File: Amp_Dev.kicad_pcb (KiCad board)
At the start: 2 copper layers, 100 x 100 mm, 508 parts, among them J1 SMA, J10 SMA, J11 CONN_01X02, J12 TEST_1P, J13 SMA, J14 CONN_01X02, J16 TEST_1P, J17 TEST_1P, J18 TEST_1P, J2 SMA, J20 SMA, J21 SMA, J22 SMA, J3 TEST_1P, J4 TEST_1P, J5 CONN_01X03, J6 TEST_1P, J7 CONN_01X03, J8 TEST_1P, J9 TEST_1P, Q1 DMN2075U, U1 MML09211H, U2 RF6886, U3 LMV358, U4 SN74LVC1G17, U5 TLV702, U6 LTC2644, U7 RT9183

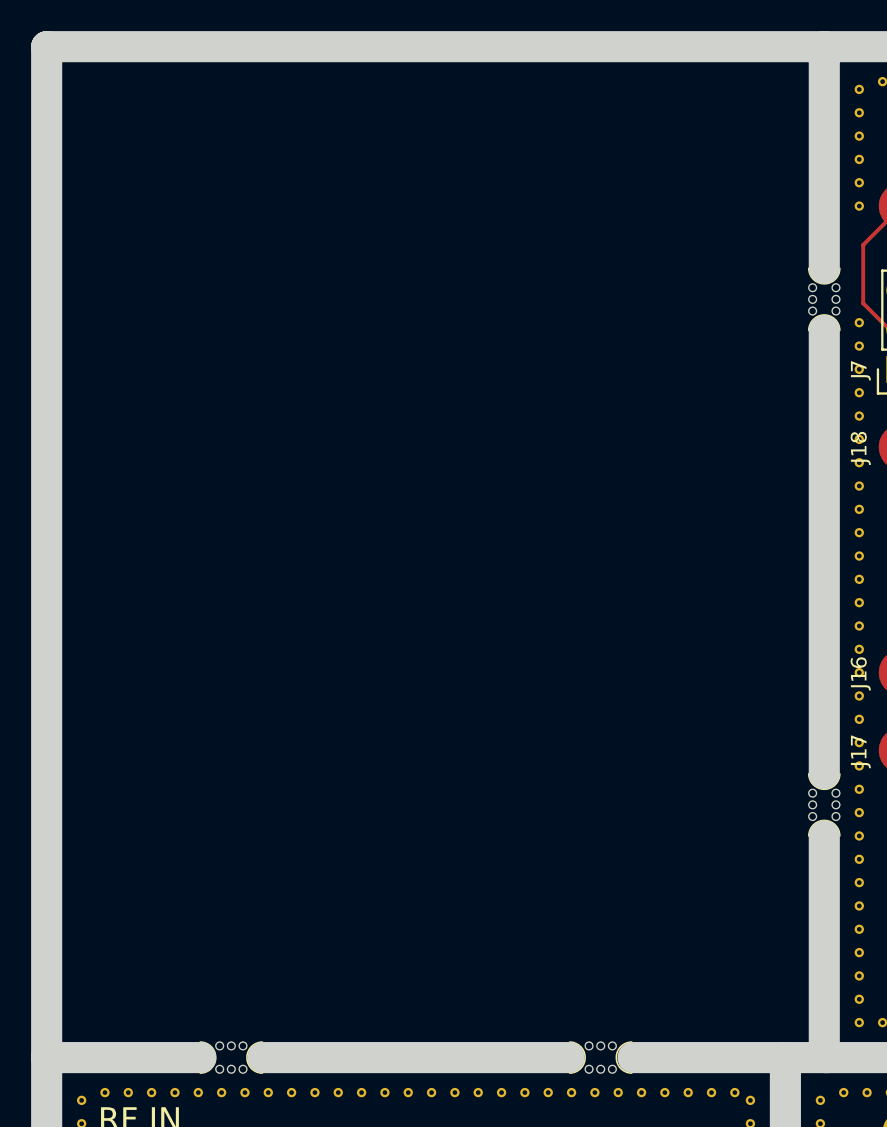
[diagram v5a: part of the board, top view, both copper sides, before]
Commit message: Added silkscreen and another PA board
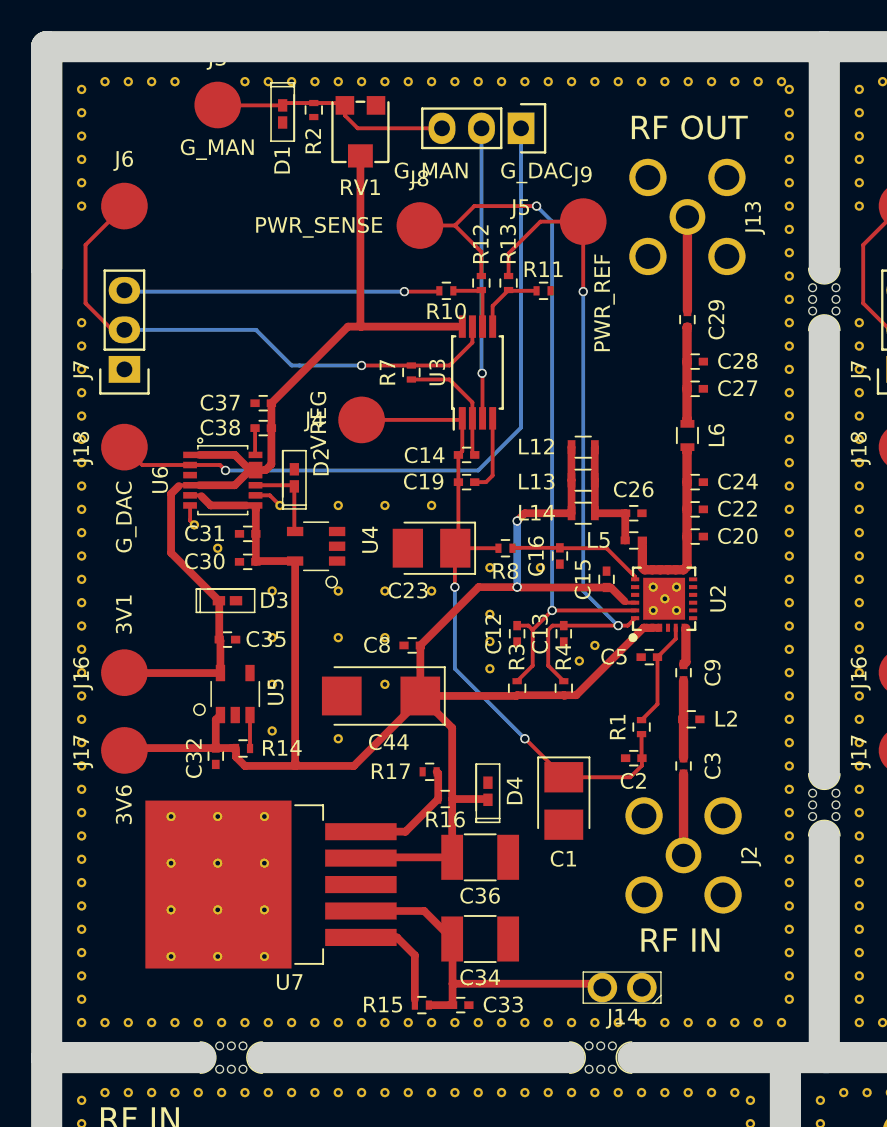
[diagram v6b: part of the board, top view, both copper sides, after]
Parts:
- added C1: 10uF, SFUSat:CP_Tantalum_Case-B_EIA-1411-21_Reflow, F.Cu at (133.2, 98.5)
- added C12: 1uF, SFUSat:C_0402, F.Cu at (130.2, 87.8)
- added C13: 1uF, SFUSat:C_0402, F.Cu at (133.2, 87.8)
- added C14: 0.1uF, SFUSat:C_0402, F.Cu at (127.0, 76.2)
- added C15: 1uF, SFUSat:C_0402, F.Cu at (136.0, 84.2)
- added C16: 2.2uF, SFUSat:C_0402, F.Cu at (133.0, 82.8)
- added C19: 1uF, SFUSat:C_0402, F.Cu at (127.0, 78.0)
- added C2: 1uF, SFUSat:C_0402, F.Cu at (137.8, 95.8)
- added C20: DNP, SFUSat:C_0402, F.Cu at (141.7, 81.5)
- added C22: 10pF, SFUSat:C_0402, F.Cu at (141.7, 79.8)
- added C23: 10uF, SFUSat:CP_Tantalum_Case-B_EIA-1411-21_Reflow, F.Cu at (124.8, 82.2)
- added C24: 27pF, SFUSat:C_0402, F.Cu at (141.7, 78.0)
- added C26: 2.2uF, SFUSat:C_0402, F.Cu at (137.8, 80.0)
- added C27: 10pF, SFUSat:C_0402, F.Cu at (141.7, 72.0)
- added C28: 1.2pF, SFUSat:C_0402, F.Cu at (141.7, 70.2)
- added C29: 100pF, SFUSat:C_0402, F.Cu at (141.2, 67.5)
- added C3: 100pF, SFUSat:C_0402, F.Cu at (140.9, 96.2)
- added C30: 0.1uF, SFUSat:C_0402, F.Cu at (112.9, 83.1)
- added C31: 0.1uF, SFUSat:C_0402, F.Cu at (112.9, 81.3)
- added C32: 1uF, SFUSat:C_0402, F.Cu at (110.9, 95.6)
- added C33: 0.1uF, SFUSat:C_0402, F.Cu at (126.6, 111.6)
- added C34: 10uF, SFUSat:C_1210, F.Cu at (127.9, 107.4)
- added C35: 1uF, SFUSat:C_0402, F.Cu at (111.6, 88.1)
- added C36: 10uF, SFUSat:C_1210, F.Cu at (127.9, 102.1)
- added C37: 0.1uF, SFUSat:C_0402, F.Cu at (113.9, 72.9)
- added C38: 0.1uF, SFUSat:C_0402, F.Cu at (113.9, 74.5)
- added C44: 10uF, SFUSat:CP_Tantalum_Case-C_EIA-2312-28_Reflow, F.Cu at (121.5, 91.8)
- added C5: 2.2uF, SFUSat:C_0402, F.Cu at (138.8, 89.2)
- added C8: 220pF, SFUSat:C_0402, F.Cu at (123.5, 88.5)
- added C9: 22pF, SFUSat:C_0402, F.Cu at (140.9, 90.2)
- added D1: PESD5Zx, SFUSat:PESD57zx, F.Cu at (115.2, 54.3)
- added D2: PESD5Zx, SFUSat:PESD57zx, F.Cu at (115.9, 77.7)
- added D3: PESD5Zx, SFUSat:PESD57zx, F.Cu at (111.6, 85.6)
- added D4: PESD5Zx, SFUSat:PESD57zx, F.Cu at (128.4, 97.9)
- added G***: LOGO, SFUSat:SFUSat_15mm_2, B.Cu at (107.8, 105.8)
- added G***: LOGO, SFUSat:SFUSat_15mm_2, B.Cu at (157.8, 105.8)
- added J13: SMA, SFUSat:SMA-Vert-TH, F.Cu at (141.2, 61.0)
- added J14: CONN_01X02, SFUSat:2x01In_Header_v2, F.Cu at (137.0, 110.5)
- added J16: TEST_1P, SFUSat:Measurement_Point_Round-SMD-Pad_Big, F.Cu at (105.0, 90.2)
- added J17: TEST_1P, SFUSat:Measurement_Point_Round-SMD-Pad_Big, F.Cu at (105.0, 95.2)
- added J18: TEST_1P, SFUSat:Measurement_Point_Round-SMD-Pad_Big, F.Cu at (105.0, 75.8)
- added J2: SMA, SFUSat:SMA-Vert-TH, F.Cu at (140.9, 102.0)
- added J3: TEST_1P, SFUSat:Measurement_Point_Round-SMD-Pad_Big, F.Cu at (111.0, 53.8)
- added J4: TEST_1P, SFUSat:Measurement_Point_Round-SMD-Pad_Big, F.Cu at (120.2, 74.0)
- added J5: CONN_01X03, SFUSat:Socket_Strip_Straight_1x03, F.Cu at (130.5, 55.2)
- added J6: TEST_1P, SFUSat:Measurement_Point_Round-SMD-Pad_Big, F.Cu at (105.0, 60.2)
- added J7: CONN_01X03, SFUSat:Socket_Strip_Straight_1x03, F.Cu at (105.0, 70.8)
- added J8: TEST_1P, SFUSat:Measurement_Point_Round-SMD-Pad_Big, F.Cu at (124.0, 61.5)
- added J9: TEST_1P, SFUSat:Measurement_Point_Round-SMD-Pad_Big, F.Cu at (134.5, 61.2)
- added L12: 0R0, SFUSat:L_0603, F.Cu at (134.5, 75.8)
- added L13: 0R0, SFUSat:L_0603, F.Cu at (134.5, 77.9)
- added L14: 0R0, SFUSat:L_0603, F.Cu at (134.5, 80.0)
- added L2: 8.2nH, SFUSat:L_0402, F.Cu at (141.4, 93.2)
- added L5: 12.55nH, SFUSat:L_0402, F.Cu at (137.8, 81.8)
- added L6: 0R0, SFUSat:L_0603, F.Cu at (141.2, 75.0)
- added R1: 220R, SFUSat:R_0402, F.Cu at (138.2, 93.8)
- added R10: 10K, SFUSat:R_0402, F.Cu at (125.7, 65.7)
- added R11: 10K, SFUSat:R_0402, F.Cu at (131.9, 65.7)
- added R12: 10K, SFUSat:R_0402, F.Cu at (128.0, 65.2)
- added R13: 10K, SFUSat:R_0402, F.Cu at (129.7, 65.2)
- added R14: 1K, SFUSat:R_0402, F.Cu at (112.6, 95.1)
- added R15: 1k, SFUSat:R_0402, F.Cu at (124.1, 111.6)
- added R16: 1k, SFUSat:R_0402, F.Cu at (125.6, 98.4)
- added R17: 287R, SFUSat:R_0402, F.Cu at (124.6, 96.6)
- added R2: 1K, SFUSat:R_0402, F.Cu at (117.2, 54.1)
- added R3: 390R, SFUSat:R_0402, F.Cu at (130.2, 91.2)
- added R4: 390R, SFUSat:R_0402, F.Cu at (133.2, 91.2)
- added R7: 1K, SFUSat:R_0402, F.Cu at (123.5, 71.0)
- added R8: 220R, SFUSat:R_0402, F.Cu at (129.5, 82.2)
- added REF**: VIA-0.6mm, SFUSat:VIA-0.6mm, F.Cu at (139.0, 84.8)
- added REF**: VIA-0.6mm, SFUSat:VIA-0.6mm, F.Cu at (102.2, 109.8)
- added REF**: VIA-0.6mm, SFUSat:VIA-0.6mm, F.Cu at (147.8, 73.8)
- added REF**: VIA-0.6mm, SFUSat:VIA-0.6mm, F.Cu at (147.8, 72.2)
- added REF**: VIA-0.6mm, SFUSat:VIA-0.6mm, F.Cu at (147.8, 70.8)
- added REF**: VIA-0.6mm, SFUSat:VIA-0.6mm, F.Cu at (147.8, 69.2)
- added REF**: VIA-0.6mm, SFUSat:VIA-0.6mm, F.Cu at (147.8, 67.8)
- added REF**: VIA-0.6mm, SFUSat:VIA-0.6mm, F.Cu at (147.8, 66.2)
- added REF**: VIA-0.6mm, SFUSat:VIA-0.6mm, F.Cu at (147.8, 64.8)
- added REF**: VIA-0.6mm, SFUSat:VIA-0.6mm, F.Cu at (147.8, 63.2)
- added REF**: VIA-0.6mm, SFUSat:VIA-0.6mm, F.Cu at (147.8, 61.8)
- added REF**: VIA-0.6mm, SFUSat:VIA-0.6mm, F.Cu at (147.8, 60.2)
- added REF**: VIA-0.6mm, SFUSat:VIA-0.6mm, F.Cu at (102.2, 108.2)
- added REF**: VIA-0.6mm, SFUSat:VIA-0.6mm, F.Cu at (147.8, 58.8)
- added REF**: VIA-0.6mm, SFUSat:VIA-0.6mm, F.Cu at (147.8, 57.2)
- added REF**: VIA-0.6mm, SFUSat:VIA-0.6mm, F.Cu at (147.8, 55.8)
- added REF**: VIA-0.6mm, SFUSat:VIA-0.6mm, F.Cu at (147.8, 54.2)
- added REF**: VIA-0.6mm, SFUSat:VIA-0.6mm, F.Cu at (147.8, 52.8)
- added REF**: VIA-0.6mm, SFUSat:VIA-0.6mm, F.Cu at (103.8, 52.2)
- added REF**: VIA-0.6mm, SFUSat:VIA-0.6mm, F.Cu at (105.2, 52.2)
- added REF**: VIA-0.6mm, SFUSat:VIA-0.6mm, F.Cu at (106.8, 52.2)
- added REF**: VIA-0.6mm, SFUSat:VIA-0.6mm, F.Cu at (108.2, 52.2)
- added REF**: VIA-0.6mm, SFUSat:VIA-0.6mm, F.Cu at (112.8, 52.2)
- added REF**: VIA-0.6mm, SFUSat:VIA-0.6mm, F.Cu at (102.2, 106.8)
- added REF**: VIA-0.6mm, SFUSat:VIA-0.6mm, F.Cu at (114.2, 52.2)
- added REF**: VIA-0.6mm, SFUSat:VIA-0.6mm, F.Cu at (115.8, 52.2)
- added REF**: VIA-0.6mm, SFUSat:VIA-0.6mm, F.Cu at (117.2, 52.2)
- added REF**: VIA-0.6mm, SFUSat:VIA-0.6mm, F.Cu at (118.8, 52.2)
- added REF**: VIA-0.6mm, SFUSat:VIA-0.6mm, F.Cu at (120.2, 52.2)
- added REF**: VIA-0.6mm, SFUSat:VIA-0.6mm, F.Cu at (121.8, 52.2)
- added REF**: VIA-0.6mm, SFUSat:VIA-0.6mm, F.Cu at (123.2, 52.2)
- added REF**: VIA-0.6mm, SFUSat:VIA-0.6mm, F.Cu at (124.8, 52.2)
- added REF**: VIA-0.6mm, SFUSat:VIA-0.6mm, F.Cu at (126.2, 52.2)
- added REF**: VIA-0.6mm, SFUSat:VIA-0.6mm, F.Cu at (127.8, 52.2)
- added REF**: VIA-0.6mm, SFUSat:VIA-0.6mm, F.Cu at (102.2, 105.2)
- added REF**: VIA-0.6mm, SFUSat:VIA-0.6mm, F.Cu at (129.2, 52.2)
- added REF**: VIA-0.6mm, SFUSat:VIA-0.6mm, F.Cu at (130.8, 52.2)
- added REF**: VIA-0.6mm, SFUSat:VIA-0.6mm, F.Cu at (132.2, 52.2)
- added REF**: VIA-0.6mm, SFUSat:VIA-0.6mm, F.Cu at (133.8, 52.2)
- added REF**: VIA-0.6mm, SFUSat:VIA-0.6mm, F.Cu at (135.2, 52.2)
- added REF**: VIA-0.6mm, SFUSat:VIA-0.6mm, F.Cu at (136.8, 52.2)
- added REF**: VIA-0.6mm, SFUSat:VIA-0.6mm, F.Cu at (138.2, 52.2)
- added REF**: VIA-0.6mm, SFUSat:VIA-0.6mm, F.Cu at (139.8, 52.2)
- added REF**: VIA-0.6mm, SFUSat:VIA-0.6mm, F.Cu at (141.2, 52.2)
- added REF**: VIA-0.6mm, SFUSat:VIA-0.6mm, F.Cu at (142.8, 52.2)
- added REF**: VIA-0.6mm, SFUSat:VIA-0.6mm, F.Cu at (102.2, 103.8)
- added REF**: VIA-0.6mm, SFUSat:VIA-0.6mm, F.Cu at (144.2, 52.2)
- added REF**: VIA-0.6mm, SFUSat:VIA-0.6mm, F.Cu at (145.8, 52.2)
- added REF**: VIA-0.6mm, SFUSat:VIA-0.6mm, F.Cu at (147.2, 52.2)
- added REF**: VIA-0.6mm, SFUSat:VIA-0.6mm, F.Cu at (128.5, 90.0)
- added REF**: VIA-0.6mm, SFUSat:VIA-0.6mm, F.Cu at (128.5, 88.2)
- added REF**: VIA-0.6mm, SFUSat:VIA-0.6mm, F.Cu at (128.5, 86.5)
- added REF**: VIA-0.6mm, SFUSat:VIA-0.6mm, F.Cu at (134.2, 89.5)
- added REF**: VIA-0.6mm, SFUSat:VIA-0.6mm, F.Cu at (128.5, 83.5)
- added REF**: VIA-0.6mm, SFUSat:VIA-0.6mm, F.Cu at (131.8, 83.5)
- added REF**: VIA-0.6mm, SFUSat:VIA-0.6mm, F.Cu at (108.0, 99.5)
- added REF**: VIA-0.6mm, SFUSat:VIA-0.6mm, F.Cu at (102.2, 102.2)
- added REF**: VIA-0.6mm, SFUSat:VIA-0.6mm, F.Cu at (111.0, 99.5)
- added REF**: VIA-0.6mm, SFUSat:VIA-0.6mm, F.Cu at (114.0, 99.5)
- added REF**: VIA-0.6mm, SFUSat:VIA-0.6mm, F.Cu at (108.0, 102.5)
- added REF**: VIA-0.6mm, SFUSat:VIA-0.6mm, F.Cu at (111.0, 102.5)
- added REF**: VIA-0.6mm, SFUSat:VIA-0.6mm, F.Cu at (114.0, 102.5)
- added REF**: VIA-0.6mm, SFUSat:VIA-0.6mm, F.Cu at (108.0, 105.5)
- added REF**: VIA-0.6mm, SFUSat:VIA-0.6mm, F.Cu at (111.0, 105.5)
- added REF**: VIA-0.6mm, SFUSat:VIA-0.6mm, F.Cu at (114.0, 105.5)
- added REF**: VIA-0.6mm, SFUSat:VIA-0.6mm, F.Cu at (108.0, 108.5)
- added REF**: VIA-0.6mm, SFUSat:VIA-0.6mm, F.Cu at (111.0, 108.5)
- added REF**: VIA-0.6mm, SFUSat:VIA-0.6mm, F.Cu at (102.2, 100.8)
- added REF**: VIA-0.6mm, SFUSat:VIA-0.6mm, F.Cu at (114.0, 108.5)
- added REF**: VIA-0.6mm, SFUSat:VIA-0.6mm, F.Cu at (109.5, 80.8)
- added REF**: VIA-0.6mm, SFUSat:VIA-0.6mm, F.Cu at (118.8, 79.5)
- added REF**: VIA-0.6mm, SFUSat:VIA-0.6mm, F.Cu at (121.8, 79.5)
- added REF**: VIA-0.6mm, SFUSat:VIA-0.6mm, F.Cu at (124.8, 79.5)
- added REF**: VIA-0.6mm, SFUSat:VIA-0.6mm, F.Cu at (118.8, 85.0)
- added REF**: VIA-0.6mm, SFUSat:VIA-0.6mm, F.Cu at (124.8, 85.0)
- added REF**: VIA-0.6mm, SFUSat:VIA-0.6mm, F.Cu at (121.8, 85.0)
- added REF**: VIA-0.6mm, SFUSat:VIA-0.6mm, F.Cu at (118.8, 88.0)
- added REF**: VIA-0.6mm, SFUSat:VIA-0.6mm, F.Cu at (121.8, 88.0)
- added REF**: VIA-0.6mm, SFUSat:VIA-0.6mm, F.Cu at (102.2, 99.2)
- added REF**: VIA-0.6mm, SFUSat:VIA-0.6mm, F.Cu at (118.8, 94.5)
- added REF**: VIA-0.6mm, SFUSat:VIA-0.6mm, F.Cu at (121.8, 91.0)
- added REF**: VIA-0.6mm, SFUSat:VIA-0.6mm, F.Cu at (111.0, 82.2)
- added REF**: VIA-0.6mm, SFUSat:VIA-0.6mm, F.Cu at (114.5, 85.0)
- added REF**: VIA-0.6mm, SFUSat:VIA-0.6mm, F.Cu at (114.5, 88.0)
- added REF**: VIA-0.6mm, SFUSat:VIA-0.6mm, F.Cu at (114.5, 91.0)
- added REF**: VIA-0.6mm, SFUSat:VIA-0.6mm, F.Cu at (114.5, 94.0)
- added REF**: VIA-0.6mm, SFUSat:VIA-0.6mm, F.Cu at (102.2, 97.8)
- added REF**: VIA-0.6mm, SFUSat:VIA-0.6mm, F.Cu at (102.2, 96.2)
- added REF**: VIA-0.6mm, SFUSat:VIA-0.6mm, F.Cu at (139.0, 86.2)
- added REF**: VIA-0.6mm, SFUSat:VIA-0.6mm, F.Cu at (102.2, 94.8)
- added REF**: VIA-0.6mm, SFUSat:VIA-0.6mm, F.Cu at (102.2, 93.2)
- added REF**: VIA-0.6mm, SFUSat:VIA-0.6mm, F.Cu at (102.2, 91.8)
- added REF**: VIA-0.6mm, SFUSat:VIA-0.6mm, F.Cu at (102.2, 90.2)
- added REF**: VIA-0.6mm, SFUSat:VIA-0.6mm, F.Cu at (102.2, 88.8)
- added REF**: VIA-0.6mm, SFUSat:VIA-0.6mm, F.Cu at (102.2, 87.2)
- added REF**: VIA-0.6mm, SFUSat:VIA-0.6mm, F.Cu at (102.2, 85.8)
- added REF**: VIA-0.6mm, SFUSat:VIA-0.6mm, F.Cu at (102.2, 84.2)
- added REF**: VIA-0.6mm, SFUSat:VIA-0.6mm, F.Cu at (102.2, 82.8)
- added REF**: VIA-0.6mm, SFUSat:VIA-0.6mm, F.Cu at (102.2, 81.2)
- added REF**: VIA-0.6mm, SFUSat:VIA-0.6mm, F.Cu at (140.5, 86.2)
- added REF**: VIA-0.6mm, SFUSat:VIA-0.6mm, F.Cu at (102.2, 79.8)
- added REF**: VIA-0.6mm, SFUSat:VIA-0.6mm, F.Cu at (102.2, 78.2)
- added REF**: VIA-0.6mm, SFUSat:VIA-0.6mm, F.Cu at (102.2, 76.8)
- added REF**: VIA-0.6mm, SFUSat:VIA-0.6mm, F.Cu at (102.2, 75.2)
- added REF**: VIA-0.6mm, SFUSat:VIA-0.6mm, F.Cu at (102.2, 73.8)
- added REF**: VIA-0.6mm, SFUSat:VIA-0.6mm, F.Cu at (102.2, 72.2)
- added REF**: VIA-0.6mm, SFUSat:VIA-0.6mm, F.Cu at (102.2, 70.8)
- added REF**: VIA-0.6mm, SFUSat:VIA-0.6mm, F.Cu at (102.2, 69.2)
- added REF**: VIA-0.6mm, SFUSat:VIA-0.6mm, F.Cu at (102.2, 67.8)
- added REF**: VIA-0.6mm, SFUSat:VIA-0.6mm, F.Cu at (102.2, 60.2)
- added REF**: VIA-0.6mm, SFUSat:VIA-0.6mm, F.Cu at (140.5, 84.8)
- added REF**: VIA-0.6mm, SFUSat:VIA-0.6mm, F.Cu at (102.2, 58.8)
- added REF**: VIA-0.6mm, SFUSat:VIA-0.6mm, F.Cu at (102.2, 57.2)
- added REF**: VIA-0.6mm, SFUSat:VIA-0.6mm, F.Cu at (102.2, 55.8)
- added REF**: VIA-0.6mm, SFUSat:VIA-0.6mm, F.Cu at (102.2, 54.2)
- added REF**: VIA-0.6mm, SFUSat:VIA-0.6mm, F.Cu at (102.2, 52.8)
- added REF**: VIA-0.6mm, SFUSat:VIA-0.6mm, F.Cu at (103.8, 112.8)
- added REF**: VIA-0.6mm, SFUSat:VIA-0.6mm, F.Cu at (105.2, 112.8)
- added REF**: VIA-0.6mm, SFUSat:VIA-0.6mm, F.Cu at (106.8, 112.8)
- added REF**: VIA-0.6mm, SFUSat:VIA-0.6mm, F.Cu at (108.2, 112.8)
- added REF**: VIA-0.6mm, SFUSat:VIA-0.6mm, F.Cu at (109.8, 112.8)
- added REF**: VIA-0.6mm, SFUSat:VIA-0.6mm, F.Cu at (139.8, 85.5)
- added REF**: VIA-0.6mm, SFUSat:VIA-0.6mm, F.Cu at (111.2, 112.8)
- added REF**: VIA-0.6mm, SFUSat:VIA-0.6mm, F.Cu at (112.8, 112.8)
- added REF**: VIA-0.6mm, SFUSat:VIA-0.6mm, F.Cu at (114.2, 112.8)
- added REF**: VIA-0.6mm, SFUSat:VIA-0.6mm, F.Cu at (115.8, 112.8)
- added REF**: VIA-0.6mm, SFUSat:VIA-0.6mm, F.Cu at (117.2, 112.8)
- added REF**: VIA-0.6mm, SFUSat:VIA-0.6mm, F.Cu at (118.8, 112.8)
- added REF**: VIA-0.6mm, SFUSat:VIA-0.6mm, F.Cu at (120.2, 112.8)
- added REF**: VIA-0.6mm, SFUSat:VIA-0.6mm, F.Cu at (121.8, 112.8)
- added REF**: VIA-0.6mm, SFUSat:VIA-0.6mm, F.Cu at (123.2, 112.8)
- added REF**: VIA-0.6mm, SFUSat:VIA-0.6mm, F.Cu at (124.8, 112.8)
- added REF**: VIA-0.6mm, SFUSat:VIA-0.6mm, F.Cu at (135.2, 88.5)
- added REF**: VIA-0.6mm, SFUSat:VIA-0.6mm, F.Cu at (126.2, 112.8)
- added REF**: VIA-0.6mm, SFUSat:VIA-0.6mm, F.Cu at (127.8, 112.8)
- added REF**: VIA-0.6mm, SFUSat:VIA-0.6mm, F.Cu at (129.2, 112.8)
- added REF**: VIA-0.6mm, SFUSat:VIA-0.6mm, F.Cu at (130.8, 112.8)
- added REF**: VIA-0.6mm, SFUSat:VIA-0.6mm, F.Cu at (132.2, 112.8)
- added REF**: VIA-0.6mm, SFUSat:VIA-0.6mm, F.Cu at (133.8, 112.8)
- added REF**: VIA-0.6mm, SFUSat:VIA-0.6mm, F.Cu at (135.2, 112.8)
- added REF**: VIA-0.6mm, SFUSat:VIA-0.6mm, F.Cu at (136.8, 112.8)
- added REF**: VIA-0.6mm, SFUSat:VIA-0.6mm, F.Cu at (138.2, 112.8)
- added REF**: VIA-0.6mm, SFUSat:VIA-0.6mm, F.Cu at (139.8, 112.8)
- added REF**: VIA-0.6mm, SFUSat:VIA-0.6mm, F.Cu at (115.0, 79.5)
- added REF**: VIA-0.6mm, SFUSat:VIA-0.6mm, F.Cu at (141.2, 112.8)
- added REF**: VIA-0.6mm, SFUSat:VIA-0.6mm, F.Cu at (142.8, 112.8)
- added REF**: VIA-0.6mm, SFUSat:VIA-0.6mm, F.Cu at (144.2, 112.8)
- added REF**: VIA-0.6mm, SFUSat:VIA-0.6mm, F.Cu at (145.8, 112.8)
- added REF**: VIA-0.6mm, SFUSat:VIA-0.6mm, F.Cu at (147.2, 112.8)
- added REF**: VIA-0.6mm, SFUSat:VIA-0.6mm, F.Cu at (147.8, 111.2)
- added REF**: VIA-0.6mm, SFUSat:VIA-0.6mm, F.Cu at (147.8, 109.8)
- added REF**: VIA-0.6mm, SFUSat:VIA-0.6mm, F.Cu at (147.8, 108.2)
- added REF**: VIA-0.6mm, SFUSat:VIA-0.6mm, F.Cu at (147.8, 106.8)
- added REF**: VIA-0.6mm, SFUSat:VIA-0.6mm, F.Cu at (147.8, 105.2)
- added REF**: VIA-0.6mm, SFUSat:VIA-0.6mm, F.Cu at (102.2, 112.8)
- added REF**: VIA-0.6mm, SFUSat:VIA-0.6mm, F.Cu at (147.8, 103.8)
- added REF**: VIA-0.6mm, SFUSat:VIA-0.6mm, F.Cu at (147.8, 102.2)
- added REF**: VIA-0.6mm, SFUSat:VIA-0.6mm, F.Cu at (147.8, 100.8)
- added REF**: VIA-0.6mm, SFUSat:VIA-0.6mm, F.Cu at (147.8, 99.2)
- added REF**: VIA-0.6mm, SFUSat:VIA-0.6mm, F.Cu at (147.8, 97.8)
- added REF**: VIA-0.6mm, SFUSat:VIA-0.6mm, F.Cu at (147.8, 96.2)
- added REF**: VIA-0.6mm, SFUSat:VIA-0.6mm, F.Cu at (147.8, 94.8)
- added REF**: VIA-0.6mm, SFUSat:VIA-0.6mm, F.Cu at (147.8, 93.2)
- added REF**: VIA-0.6mm, SFUSat:VIA-0.6mm, F.Cu at (147.8, 91.8)
- added REF**: VIA-0.6mm, SFUSat:VIA-0.6mm, F.Cu at (147.8, 90.2)
- added REF**: VIA-0.6mm, SFUSat:VIA-0.6mm, F.Cu at (102.2, 111.2)
- added REF**: VIA-0.6mm, SFUSat:VIA-0.6mm, F.Cu at (147.8, 88.8)
- added REF**: VIA-0.6mm, SFUSat:VIA-0.6mm, F.Cu at (147.8, 87.2)
- added REF**: VIA-0.6mm, SFUSat:VIA-0.6mm, F.Cu at (147.8, 85.8)
- added REF**: VIA-0.6mm, SFUSat:VIA-0.6mm, F.Cu at (147.8, 84.2)
- added REF**: VIA-0.6mm, SFUSat:VIA-0.6mm, F.Cu at (147.8, 82.8)
- added REF**: VIA-0.6mm, SFUSat:VIA-0.6mm, F.Cu at (147.8, 81.2)
- added REF**: VIA-0.6mm, SFUSat:VIA-0.6mm, F.Cu at (147.8, 79.8)
- added REF**: VIA-0.6mm, SFUSat:VIA-0.6mm, F.Cu at (147.8, 78.2)
- added REF**: VIA-0.6mm, SFUSat:VIA-0.6mm, F.Cu at (147.8, 76.8)
- added REF**: VIA-0.6mm, SFUSat:VIA-0.6mm, F.Cu at (147.8, 75.2)
- added RV1: POT, SFUSat:TC33_SMD, F.Cu at (120.2, 55.6)
- added U2: RF6886, SFUSat:QFN-24, F.Cu at (139.7, 85.5)
- added U3: LMV358, SFUSat:TSSOP-8_4.4x3mm_Pitch0.65mm, F.Cu at (127.7, 71.0)
- added U4: SN74LVC1G17, SFUSat:SOT_23_5, F.Cu at (117.3, 82.1)
- added U5: TLV702, SFUSat:SOT_23_5, F.Cu at (112.1, 91.6)
- added U6: LTC2644, SFUSat:12-TSSOP, F.Cu at (111.3, 77.9)
- added U7: RT9183, SFUSat:TO-263-5Lead, F.Cu at (115.6, 103.9)
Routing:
- net /3V6: track 117.1 -> 234.1 mm, vias 2 -> 4
- net /3V1: track 60.7 -> 121.3 mm
- net /PWR_SENSE: track 50.3 -> 100.6 mm, vias 2 -> 4
- net /G_DAC: track 46.5 -> 93.0 mm, vias 1 -> 2
- net /PWR_REF: track 43.7 -> 87.3 mm, vias 2 -> 4
- net /VREG: track 42.9 -> 85.8 mm, vias 2 -> 4
- net Net-(J6-Pad1): track 35.5 -> 70.9 mm, vias 1 -> 2
- net Net-(C33-Pad1): track 22.1 -> 44.3 mm
- net Net-(J7-Pad3): track 20.3 -> 40.6 mm, vias 1 -> 2
- net Net-(J5-Pad2): track 18.7 -> 37.4 mm, vias 1 -> 2
- net /G_MAN: track 15.5 -> 31.1 mm
- net Net-(C20-Pad1): track 12.5 -> 24.9 mm
- net GND: track 17.1 -> 27.0 mm
- net Net-(C16-Pad1): track 8.87 -> 17.7 mm
- net Net-(C26-Pad1): track 7.99 -> 16.0 mm
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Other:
- outline, holes or cut-outs redrawn
- board text added: "CubeSat Radio PA Eval R1 SFU Satellite Design Team July 2017"
